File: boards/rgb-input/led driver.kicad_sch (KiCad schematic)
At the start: 4 parts, among them U6 TLC5947DAP

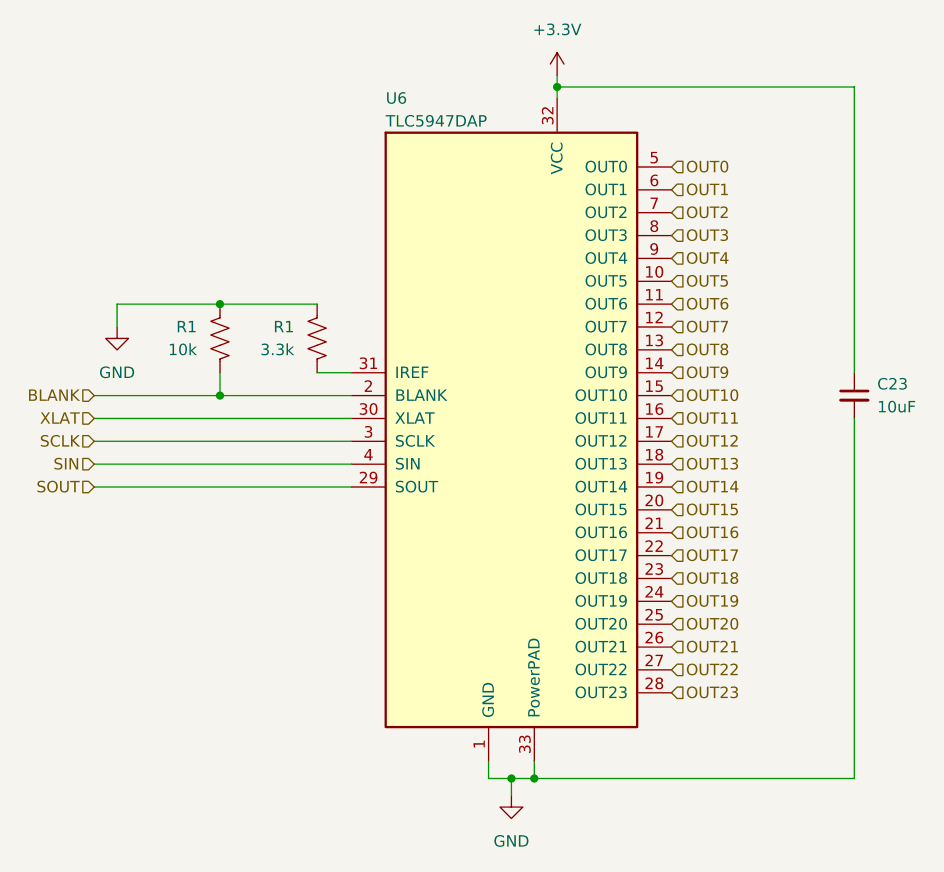
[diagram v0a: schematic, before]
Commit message: tested the bus voltage stuff a bit more
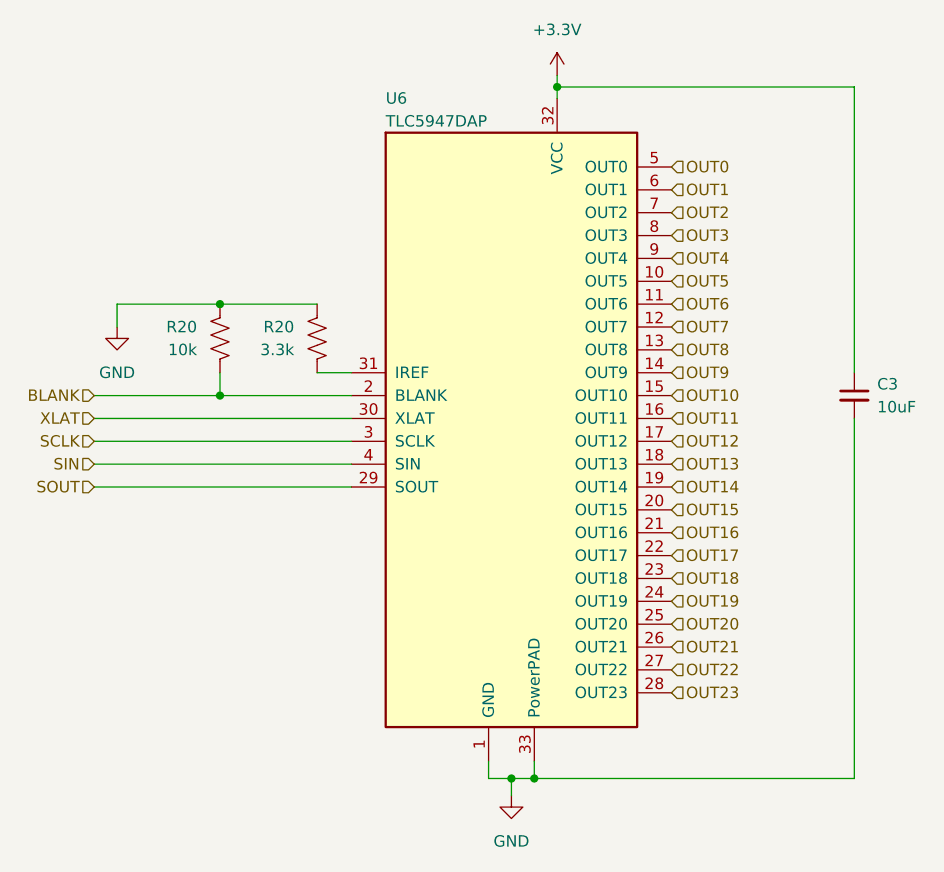
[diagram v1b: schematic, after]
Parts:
- renumbered C23 to C3, R1 to R20

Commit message: some adc changes and then rerouting
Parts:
- renumbered R20 to R1
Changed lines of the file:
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@@
   (symbol (lib_id "Device:R_US") (at 95.25 80.01 0) (mirror x) (unit 1)
     (in_bom yes) (on_board yes) (dnp no) (fields_autoplaced)
-    (property "Reference" "R20" (at 92.71 78.74 0)
+    (property "Reference" "R1" (at 92.71 78.74 0)
       (effects (font (size 1.27 1.27)) (justify right))
     )
@@
     (instances
       (project "rgb-input"
+        (path "/c83c6236-96e9-46ad-9d7a-9e2efa4a7966/ef548cdc-9d5d-4f8e-8f54-0c2e96dbe3f0"
+          (reference "R1") (unit 1)
+        )
+        (path "/c83c6236-96e9-46ad-9d7a-9e2efa4a7966/4f50afed-9381-4977-8e27-209f0f88ad4e"
+          (reference "R3") (unit 1)
+        )
+        (path "/c83c6236-96e9-46ad-9d7a-9e2efa4a7966/4175a172-5c0b-4d6a-88bb-129f5f07b813"
+          (reference "R5") (unit 1)
+        )
+        (path "/c83c6236-96e9-46ad-9d7a-9e2efa4a7966/6f6f2d8d-82f6-4691-bba7-8caa1bd52e96"
+          (reference "R7") (unit 1)
+        )
+        (path "/c83c6236-96e9-46ad-9d7a-9e2efa4a7966/145fa34f-e19e-43e2-bb48-aff2e824ef0a"
+          (reference "R9") (unit 1)
+        )
+        (path "/c83c6236-96e9-46ad-9d7a-9e2efa4a7966/5fc618b8-7830-4bbf-bf46-7753631e9b1e"
+          (reference "R11") (unit 1)
+        )
+        (path "/c83c6236-96e9-46ad-9d7a-9e2efa4a7966/f06c9bf0-de4e-49a2-91ec-1c9426377826"
+          (reference "R19") (unit 1)
+        )
+        (path "/c83c6236-96e9-46ad-9d7a-9e2efa4a7966/803edf1a-5825-4947-a8b9-85d3a29697e5"
+          (reference "R15") (unit 1)
+        )
+        (path "/c83c6236-96e9-46ad-9d7a-9e2efa4a7966/a581b924-afd8-4b56-b69e-790286072066"
+          (reference "R17") (unit 1)
+        )
         (path "/c83c6236-96e9-46ad-9d7a-9e2efa4a7966/120468c6-3bec-414c-9049-57af589f397a"
           (reference "R20") (unit 1)
         )
-        (path "/c83c6236-96e9-46ad-9d7a-9e2efa4a7966/4f50afed-9381-4977-8e27-209f0f88ad4e"
-          (reference "R3") (unit 1)
-        )
-        (path "/c83c6236-96e9-46ad-9d7a-9e2efa4a7966/4175a172-5c0b-4d6a-88bb-129f5f07b813"
-          (reference "R5") (unit 1)
-        )
-        (path "/c83c6236-96e9-46ad-9d7a-9e2efa4a7966/6f6f2d8d-82f6-4691-bba7-8caa1bd52e96"
-          (reference "R7") (unit 1)
-        )
-        (path "/c83c6236-96e9-46ad-9d7a-9e2efa4a7966/145fa34f-e19e-43e2-bb48-aff2e824ef0a"
-          (reference "R9") (unit 1)
-        )
-        (path "/c83c6236-96e9-46ad-9d7a-9e2efa4a7966/5fc618b8-7830-4bbf-bf46-7753631e9b1e"
-          (reference "R11") (unit 1)
-        )
-        (path "/c83c6236-96e9-46ad-9d7a-9e2efa4a7966/f06c9bf0-de4e-49a2-91ec-1c9426377826"
-          (reference "R19") (unit 1)
-        )
-        (path "/c83c6236-96e9-46ad-9d7a-9e2efa4a7966/803edf1a-5825-4947-a8b9-85d3a29697e5"
-          (reference "R15") (unit 1)
-        )
-        (path "/c83c6236-96e9-46ad-9d7a-9e2efa4a7966/a581b924-afd8-4b56-b69e-790286072066"
-          (reference "R17") (unit 1)
-        )
         (path "/c83c6236-96e9-46ad-9d7a-9e2efa4a7966/802175d5-fb4b-4457-a117-b0f397189ff7"
           (reference "R13") (unit 1)
-        )
-        (path "/c83c6236-96e9-46ad-9d7a-9e2efa4a7966/ef548cdc-9d5d-4f8e-8f54-0c2e96dbe3f0"
-          (reference "R1") (unit 1)
         )
         (path "/c83c6236-96e9-46ad-9d7a-9e2efa4a7966/c9e1b2da-9064-45a5-a0a2-ee072f7e1acf"
@@
   (symbol (lib_id "Device:R_US") (at 84.455 80.01 0) (mirror x) (unit 1)
     (in_bom yes) (on_board yes) (dnp no) (fields_autoplaced)
-    (property "Reference" "R20" (at 81.915 78.74 0)
+    (property "Reference" "R1" (at 81.915 78.74 0)
       (effects (font (size 1.27 1.27)) (justify right))
     )
@@
     (instances
       (project "rgb-input"
+        (path "/c83c6236-96e9-46ad-9d7a-9e2efa4a7966/ef548cdc-9d5d-4f8e-8f54-0c2e96dbe3f0"
+          (reference "R1") (unit 1)
+        )
+        (path "/c83c6236-96e9-46ad-9d7a-9e2efa4a7966/4f50afed-9381-4977-8e27-209f0f88ad4e"
+          (reference "R3") (unit 1)
+        )
+        (path "/c83c6236-96e9-46ad-9d7a-9e2efa4a7966/4175a172-5c0b-4d6a-88bb-129f5f07b813"
+          (reference "R5") (unit 1)
+        )
+        (path "/c83c6236-96e9-46ad-9d7a-9e2efa4a7966/6f6f2d8d-82f6-4691-bba7-8caa1bd52e96"
+          (reference "R7") (unit 1)
+        )
+        (path "/c83c6236-96e9-46ad-9d7a-9e2efa4a7966/145fa34f-e19e-43e2-bb48-aff2e824ef0a"
+          (reference "R9") (unit 1)
+        )
+        (path "/c83c6236-96e9-46ad-9d7a-9e2efa4a7966/5fc618b8-7830-4bbf-bf46-7753631e9b1e"
+          (reference "R11") (unit 1)
+        )
+        (path "/c83c6236-96e9-46ad-9d7a-9e2efa4a7966/f06c9bf0-de4e-49a2-91ec-1c9426377826"
+          (reference "R19") (unit 1)
+        )
+        (path "/c83c6236-96e9-46ad-9d7a-9e2efa4a7966/803edf1a-5825-4947-a8b9-85d3a29697e5"
+          (reference "R15") (unit 1)
+        )
+        (path "/c83c6236-96e9-46ad-9d7a-9e2efa4a7966/a581b924-afd8-4b56-b69e-790286072066"
+          (reference "R17") (unit 1)
+        )
         (path "/c83c6236-96e9-46ad-9d7a-9e2efa4a7966/120468c6-3bec-414c-9049-57af589f397a"
           (reference "R20") (unit 1)
         )
-        (path "/c83c6236-96e9-46ad-9d7a-9e2efa4a7966/4f50afed-9381-4977-8e27-209f0f88ad4e"
-          (reference "R3") (unit 1)
-        )
-        (path "/c83c6236-96e9-46ad-9d7a-9e2efa4a7966/4175a172-5c0b-4d6a-88bb-129f5f07b813"
-          (reference "R5") (unit 1)
-        )
-        (path "/c83c6236-96e9-46ad-9d7a-9e2efa4a7966/6f6f2d8d-82f6-4691-bba7-8caa1bd52e96"
-          (reference "R7") (unit 1)
-        )
-        (path "/c83c6236-96e9-46ad-9d7a-9e2efa4a7966/145fa34f-e19e-43e2-bb48-aff2e824ef0a"
-          (reference "R9") (unit 1)
-        )
-        (path "/c83c6236-96e9-46ad-9d7a-9e2efa4a7966/5fc618b8-7830-4bbf-bf46-7753631e9b1e"
-          (reference "R11") (unit 1)
-        )
-        (path "/c83c6236-96e9-46ad-9d7a-9e2efa4a7966/f06c9bf0-de4e-49a2-91ec-1c9426377826"
-          (reference "R19") (unit 1)
-        )
-        (path "/c83c6236-96e9-46ad-9d7a-9e2efa4a7966/803edf1a-5825-4947-a8b9-85d3a29697e5"
-          (reference "R15") (unit 1)
-        )
-        (path "/c83c6236-96e9-46ad-9d7a-9e2efa4a7966/a581b924-afd8-4b56-b69e-790286072066"
-          (reference "R17") (unit 1)
-        )
         (path "/c83c6236-96e9-46ad-9d7a-9e2efa4a7966/802175d5-fb4b-4457-a117-b0f397189ff7"
           (reference "R13") (unit 1)
         )
-        (path "/c83c6236-96e9-46ad-9d7a-9e2efa4a7966/ef548cdc-9d5d-4f8e-8f54-0c2e96dbe3f0"
-          (reference "R1") (unit 1)
-        )
         (path "/c83c6236-96e9-46ad-9d7a-9e2efa4a7966/c9e1b2da-9064-45a5-a0a2-ee072f7e1acf"

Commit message: figured out most of the components, working on placement
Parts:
- renumbered R1 to R13
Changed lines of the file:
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@@
   (symbol (lib_id "Device:R_US") (at 95.25 80.01 0) (mirror x) (unit 1)
     (in_bom yes) (on_board yes) (dnp no) (fields_autoplaced)
-    (property "Reference" "R1" (at 92.71 78.74 0)
+    (property "Reference" "R13" (at 92.71 78.74 0)
       (effects (font (size 1.27 1.27)) (justify right))
     )
@@
     (instances
       (project "rgb-input"
+        (path "/c83c6236-96e9-46ad-9d7a-9e2efa4a7966/802175d5-fb4b-4457-a117-b0f397189ff7"
+          (reference "R13") (unit 1)
+        )
+        (path "/c83c6236-96e9-46ad-9d7a-9e2efa4a7966/4f50afed-9381-4977-8e27-209f0f88ad4e"
+          (reference "R3") (unit 1)
+        )
+        (path "/c83c6236-96e9-46ad-9d7a-9e2efa4a7966/4175a172-5c0b-4d6a-88bb-129f5f07b813"
+          (reference "R5") (unit 1)
+        )
+        (path "/c83c6236-96e9-46ad-9d7a-9e2efa4a7966/6f6f2d8d-82f6-4691-bba7-8caa1bd52e96"
+          (reference "R7") (unit 1)
+        )
+        (path "/c83c6236-96e9-46ad-9d7a-9e2efa4a7966/145fa34f-e19e-43e2-bb48-aff2e824ef0a"
+          (reference "R9") (unit 1)
+        )
+        (path "/c83c6236-96e9-46ad-9d7a-9e2efa4a7966/5fc618b8-7830-4bbf-bf46-7753631e9b1e"
+          (reference "R11") (unit 1)
+        )
+        (path "/c83c6236-96e9-46ad-9d7a-9e2efa4a7966/f06c9bf0-de4e-49a2-91ec-1c9426377826"
+          (reference "R19") (unit 1)
+        )
+        (path "/c83c6236-96e9-46ad-9d7a-9e2efa4a7966/803edf1a-5825-4947-a8b9-85d3a29697e5"
+          (reference "R15") (unit 1)
+        )
+        (path "/c83c6236-96e9-46ad-9d7a-9e2efa4a7966/a581b924-afd8-4b56-b69e-790286072066"
+          (reference "R17") (unit 1)
+        )
         (path "/c83c6236-96e9-46ad-9d7a-9e2efa4a7966/ef548cdc-9d5d-4f8e-8f54-0c2e96dbe3f0"
           (reference "R1") (unit 1)
         )
-        (path "/c83c6236-96e9-46ad-9d7a-9e2efa4a7966/4f50afed-9381-4977-8e27-209f0f88ad4e"
-          (reference "R3") (unit 1)
-        )
-        (path "/c83c6236-96e9-46ad-9d7a-9e2efa4a7966/4175a172-5c0b-4d6a-88bb-129f5f07b813"
-          (reference "R5") (unit 1)
-        )
-        (path "/c83c6236-96e9-46ad-9d7a-9e2efa4a7966/6f6f2d8d-82f6-4691-bba7-8caa1bd52e96"
-          (reference "R7") (unit 1)
-        )
-        (path "/c83c6236-96e9-46ad-9d7a-9e2efa4a7966/145fa34f-e19e-43e2-bb48-aff2e824ef0a"
-          (reference "R9") (unit 1)
-        )
-        (path "/c83c6236-96e9-46ad-9d7a-9e2efa4a7966/5fc618b8-7830-4bbf-bf46-7753631e9b1e"
-          (reference "R11") (unit 1)
-        )
-        (path "/c83c6236-96e9-46ad-9d7a-9e2efa4a7966/f06c9bf0-de4e-49a2-91ec-1c9426377826"
-          (reference "R19") (unit 1)
-        )
-        (path "/c83c6236-96e9-46ad-9d7a-9e2efa4a7966/803edf1a-5825-4947-a8b9-85d3a29697e5"
-          (reference "R15") (unit 1)
-        )
-        (path "/c83c6236-96e9-46ad-9d7a-9e2efa4a7966/a581b924-afd8-4b56-b69e-790286072066"
-          (reference "R17") (unit 1)
-        )
         (path "/c83c6236-96e9-46ad-9d7a-9e2efa4a7966/120468c6-3bec-414c-9049-57af589f397a"
           (reference "R20") (unit 1)
-        )
-        (path "/c83c6236-96e9-46ad-9d7a-9e2efa4a7966/802175d5-fb4b-4457-a117-b0f397189ff7"
-          (reference "R13") (unit 1)
         )
         (path "/c83c6236-96e9-46ad-9d7a-9e2efa4a7966/c9e1b2da-9064-45a5-a0a2-ee072f7e1acf"
@@
   (symbol (lib_id "Device:R_US") (at 84.455 80.01 0) (mirror x) (unit 1)
     (in_bom yes) (on_board yes) (dnp no) (fields_autoplaced)
-    (property "Reference" "R1" (at 81.915 78.74 0)
+    (property "Reference" "R13" (at 81.915 78.74 0)
       (effects (font (size 1.27 1.27)) (justify right))
     )
@@
     (instances
       (project "rgb-input"
+        (path "/c83c6236-96e9-46ad-9d7a-9e2efa4a7966/802175d5-fb4b-4457-a117-b0f397189ff7"
+          (reference "R13") (unit 1)
+        )
+        (path "/c83c6236-96e9-46ad-9d7a-9e2efa4a7966/4f50afed-9381-4977-8e27-209f0f88ad4e"
+          (reference "R3") (unit 1)
+        )
+        (path "/c83c6236-96e9-46ad-9d7a-9e2efa4a7966/4175a172-5c0b-4d6a-88bb-129f5f07b813"
+          (reference "R5") (unit 1)
+        )
+        (path "/c83c6236-96e9-46ad-9d7a-9e2efa4a7966/6f6f2d8d-82f6-4691-bba7-8caa1bd52e96"
+          (reference "R7") (unit 1)
+        )
+        (path "/c83c6236-96e9-46ad-9d7a-9e2efa4a7966/145fa34f-e19e-43e2-bb48-aff2e824ef0a"
+          (reference "R9") (unit 1)
+        )
+        (path "/c83c6236-96e9-46ad-9d7a-9e2efa4a7966/5fc618b8-7830-4bbf-bf46-7753631e9b1e"
+          (reference "R11") (unit 1)
+        )
+        (path "/c83c6236-96e9-46ad-9d7a-9e2efa4a7966/f06c9bf0-de4e-49a2-91ec-1c9426377826"
+          (reference "R19") (unit 1)
+        )
+        (path "/c83c6236-96e9-46ad-9d7a-9e2efa4a7966/803edf1a-5825-4947-a8b9-85d3a29697e5"
+          (reference "R15") (unit 1)
+        )
+        (path "/c83c6236-96e9-46ad-9d7a-9e2efa4a7966/a581b924-afd8-4b56-b69e-790286072066"
+          (reference "R17") (unit 1)
+        )
         (path "/c83c6236-96e9-46ad-9d7a-9e2efa4a7966/ef548cdc-9d5d-4f8e-8f54-0c2e96dbe3f0"
           (reference "R1") (unit 1)
         )
-        (path "/c83c6236-96e9-46ad-9d7a-9e2efa4a7966/4f50afed-9381-4977-8e27-209f0f88ad4e"
-          (reference "R3") (unit 1)
-        )
-        (path "/c83c6236-96e9-46ad-9d7a-9e2efa4a7966/4175a172-5c0b-4d6a-88bb-129f5f07b813"
-          (reference "R5") (unit 1)
-        )
-        (path "/c83c6236-96e9-46ad-9d7a-9e2efa4a7966/6f6f2d8d-82f6-4691-bba7-8caa1bd52e96"
-          (reference "R7") (unit 1)
-        )
-        (path "/c83c6236-96e9-46ad-9d7a-9e2efa4a7966/145fa34f-e19e-43e2-bb48-aff2e824ef0a"
-          (reference "R9") (unit 1)
-        )
-        (path "/c83c6236-96e9-46ad-9d7a-9e2efa4a7966/5fc618b8-7830-4bbf-bf46-7753631e9b1e"
-          (reference "R11") (unit 1)
-        )
-        (path "/c83c6236-96e9-46ad-9d7a-9e2efa4a7966/f06c9bf0-de4e-49a2-91ec-1c9426377826"
-          (reference "R19") (unit 1)
-        )
-        (path "/c83c6236-96e9-46ad-9d7a-9e2efa4a7966/803edf1a-5825-4947-a8b9-85d3a29697e5"
-          (reference "R15") (unit 1)
-        )
-        (path "/c83c6236-96e9-46ad-9d7a-9e2efa4a7966/a581b924-afd8-4b56-b69e-790286072066"
-          (reference "R17") (unit 1)
-        )
         (path "/c83c6236-96e9-46ad-9d7a-9e2efa4a7966/120468c6-3bec-414c-9049-57af589f397a"
           (reference "R20") (unit 1)
         )
-        (path "/c83c6236-96e9-46ad-9d7a-9e2efa4a7966/802175d5-fb4b-4457-a117-b0f397189ff7"
-          (reference "R13") (unit 1)
-        )
         (path "/c83c6236-96e9-46ad-9d7a-9e2efa4a7966/c9e1b2da-9064-45a5-a0a2-ee072f7e1acf"

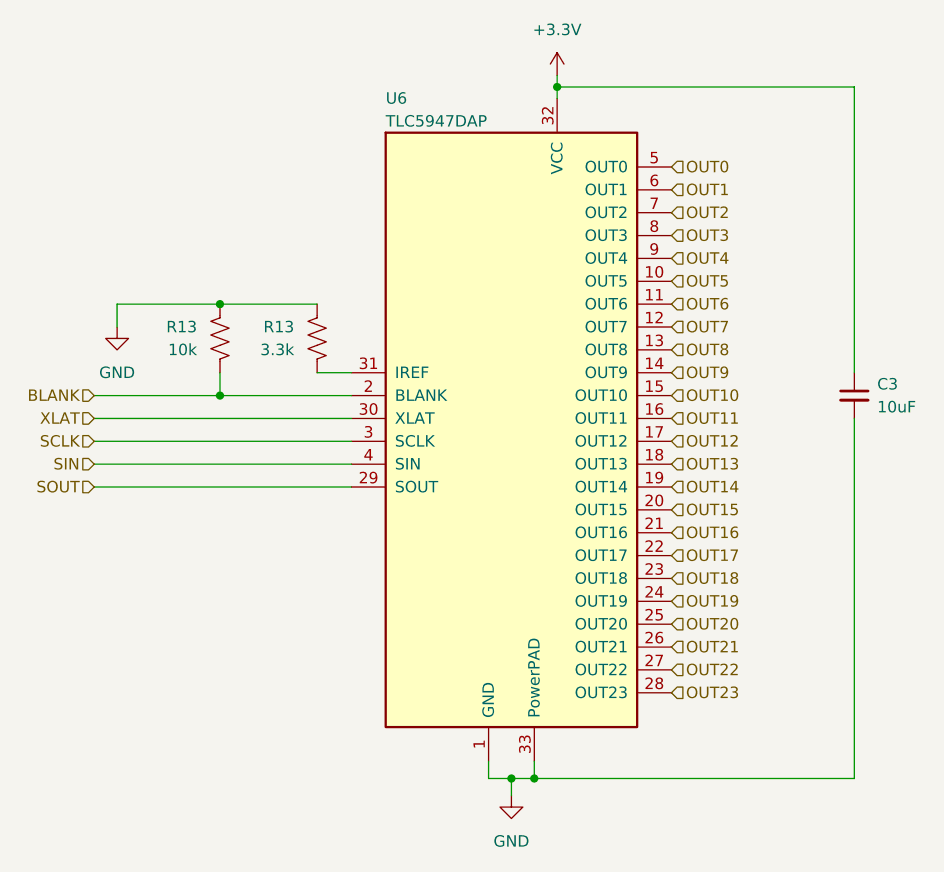
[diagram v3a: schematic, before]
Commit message: more layout checks on the input board
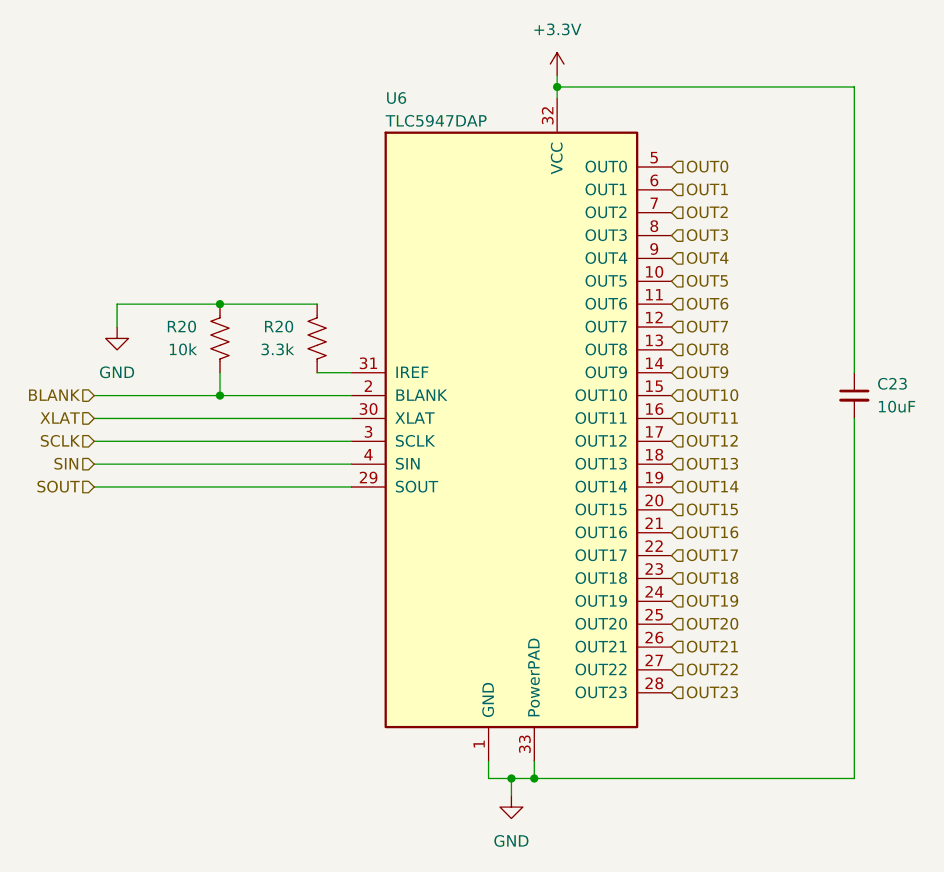
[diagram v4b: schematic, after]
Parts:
- renumbered C3 to C23, R13 to R20
